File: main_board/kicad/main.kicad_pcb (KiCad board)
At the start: 2 copper layers, 200 x 150 mm, 148 parts, among them J1 Sensorbuchse, J2 Motorbuchse, J3 Motorbuchse, J4 Batteriebuchse, J5 Conn_02x07_Odd_Even, J6 Sensorbuchse, J7 AVR-ISP-10, Q1 IRFB3077, Q13 IRFB3077, Q14 IRFB3077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

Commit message: rerouted some lines, also added attiny
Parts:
- moved R3 316.3 mm to (40.0, 89.5), turned to 0 degrees
- moved R2 311.5 mm to (31.1, 90.2), turned to 90 degrees
- moved C3 311.2 mm to (34.9, 74.3), turned to 0 degrees
- moved U2 300.9 mm to (42.6, 85.1)
- moved R1 297.3 mm to (45.7, 69.8), turned to -90 degrees
- moved C4 292.1 mm to (42.5, 74.3), turned to 180 degrees
- moved J7 214.9 mm to (132.1, 34.3), turned to 90 degrees
- moved J1 133.5 mm to (219.6, 158.8), turned to 90 degrees
- moved J6 106.3 mm to (219.1, 52.1), turned to 90 degrees
- moved C22 65.7 mm to (163.2, 166.3), turned to 90 degrees
- moved C24 48.8 mm to (185.4, 75.6), turned to -90 degrees
- moved R26 47.7 mm to (175.9, 80.6), turned to 90 degrees
- moved C17 47.5 mm to (188.6, 75.6), turned to -90 degrees
- moved R28 46.8 mm to (185.4, 65.4), turned to -90 degrees
- moved C20 44.9 mm to (182.2, 70.4), turned to 90 degrees
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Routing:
- net +5V: track 74.1 -> 298.1 mm
- net GND: track 947.0 -> 1155.3 mm
- net /attiny13/SCK: track 0.00 -> 160.3 mm
- net /MotorMagic_R/HAL1: track 0.00 -> 101.1 mm
- net /MotorMagic_R/HAL2: track 0.00 -> 93.8 mm
- net /MotorMagic_R/HAL3: track 0.00 -> 88.6 mm
- net Net-(U5-A0): track 5.18 -> 68.4 mm
- net Net-(U5-A1): track 5.61 -> 65.1 mm
- net Net-(U5-A2): track 6.13 -> 62.9 mm
- net /BAT_CHARGE_PWM: track 0.00 -> 53.8 mm
- net /MotorMagic_R/bridge2/Y_L: track 74.5 -> 118.5 mm
- net /MotorMagic_L/HAL3: track 0.00 -> 43.8 mm
- net /MotorMagic_R/bridge2/Y_H: track 62.9 -> 104.9 mm
- net /MotorMagic_R/bridge2/G_H: track 87.9 -> 129.0 mm
- net /MotorMagic_R/bridge2/B_H: track 112.7 -> 153.6 mm
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
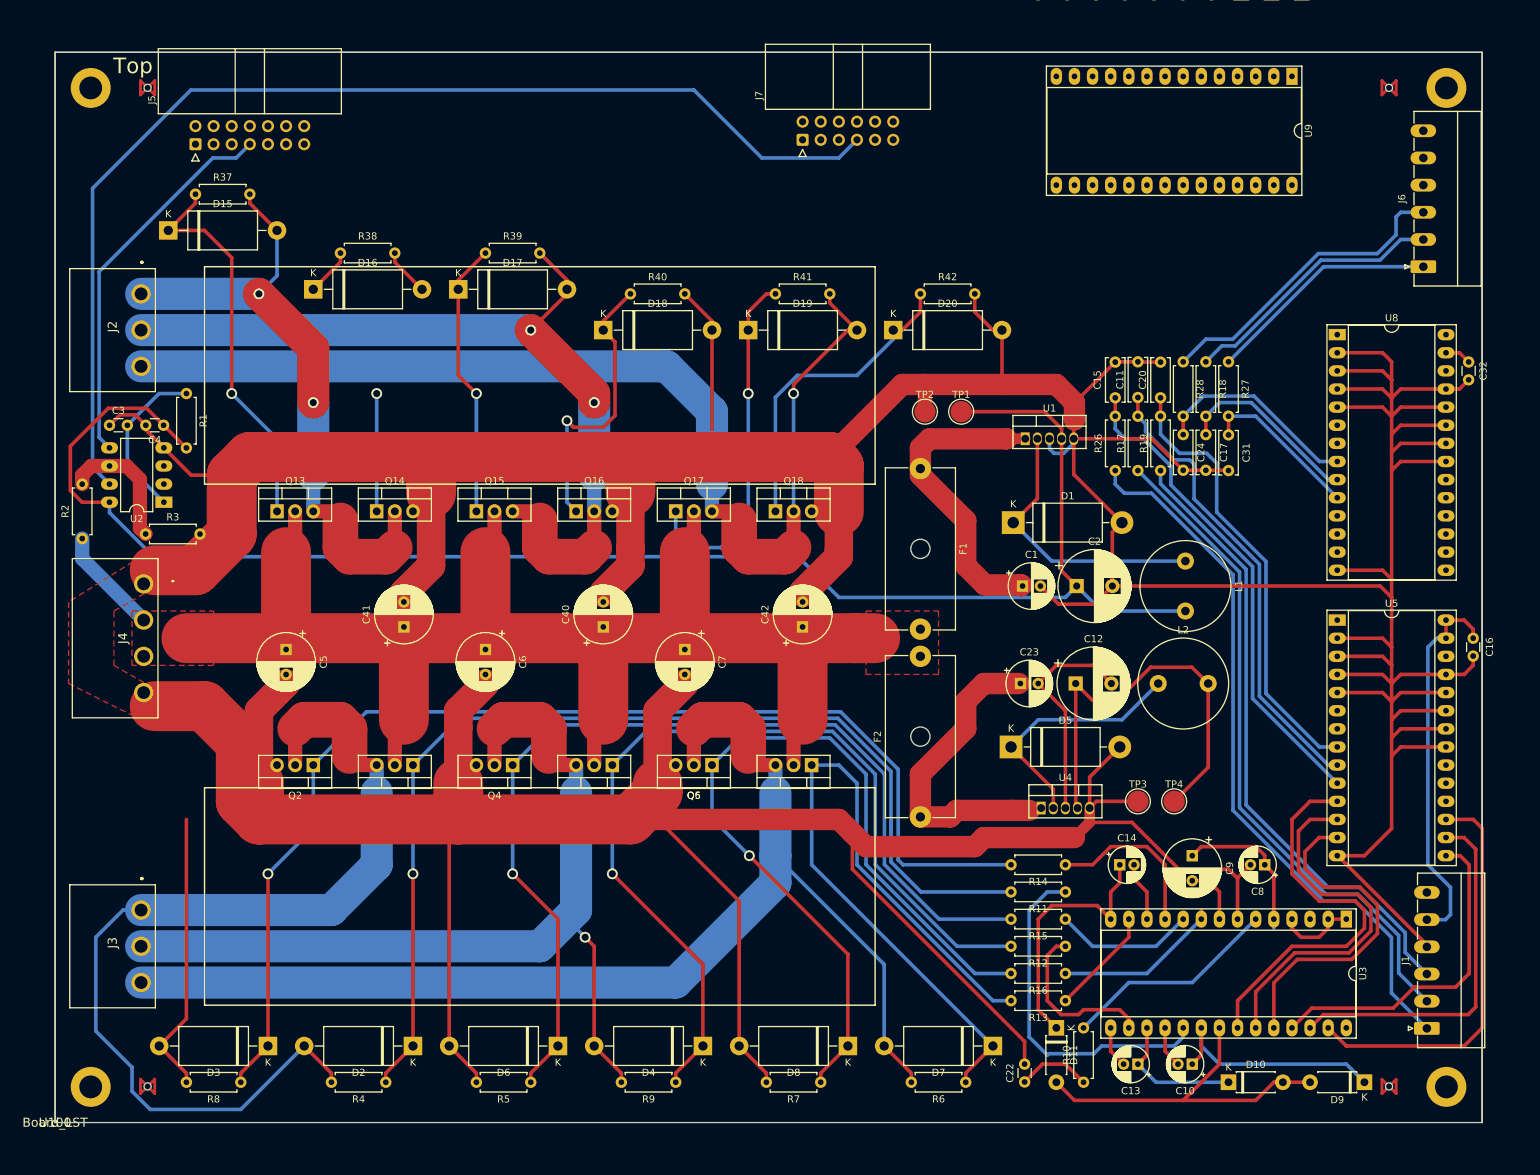
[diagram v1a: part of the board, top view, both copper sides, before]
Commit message: rerouted some lines
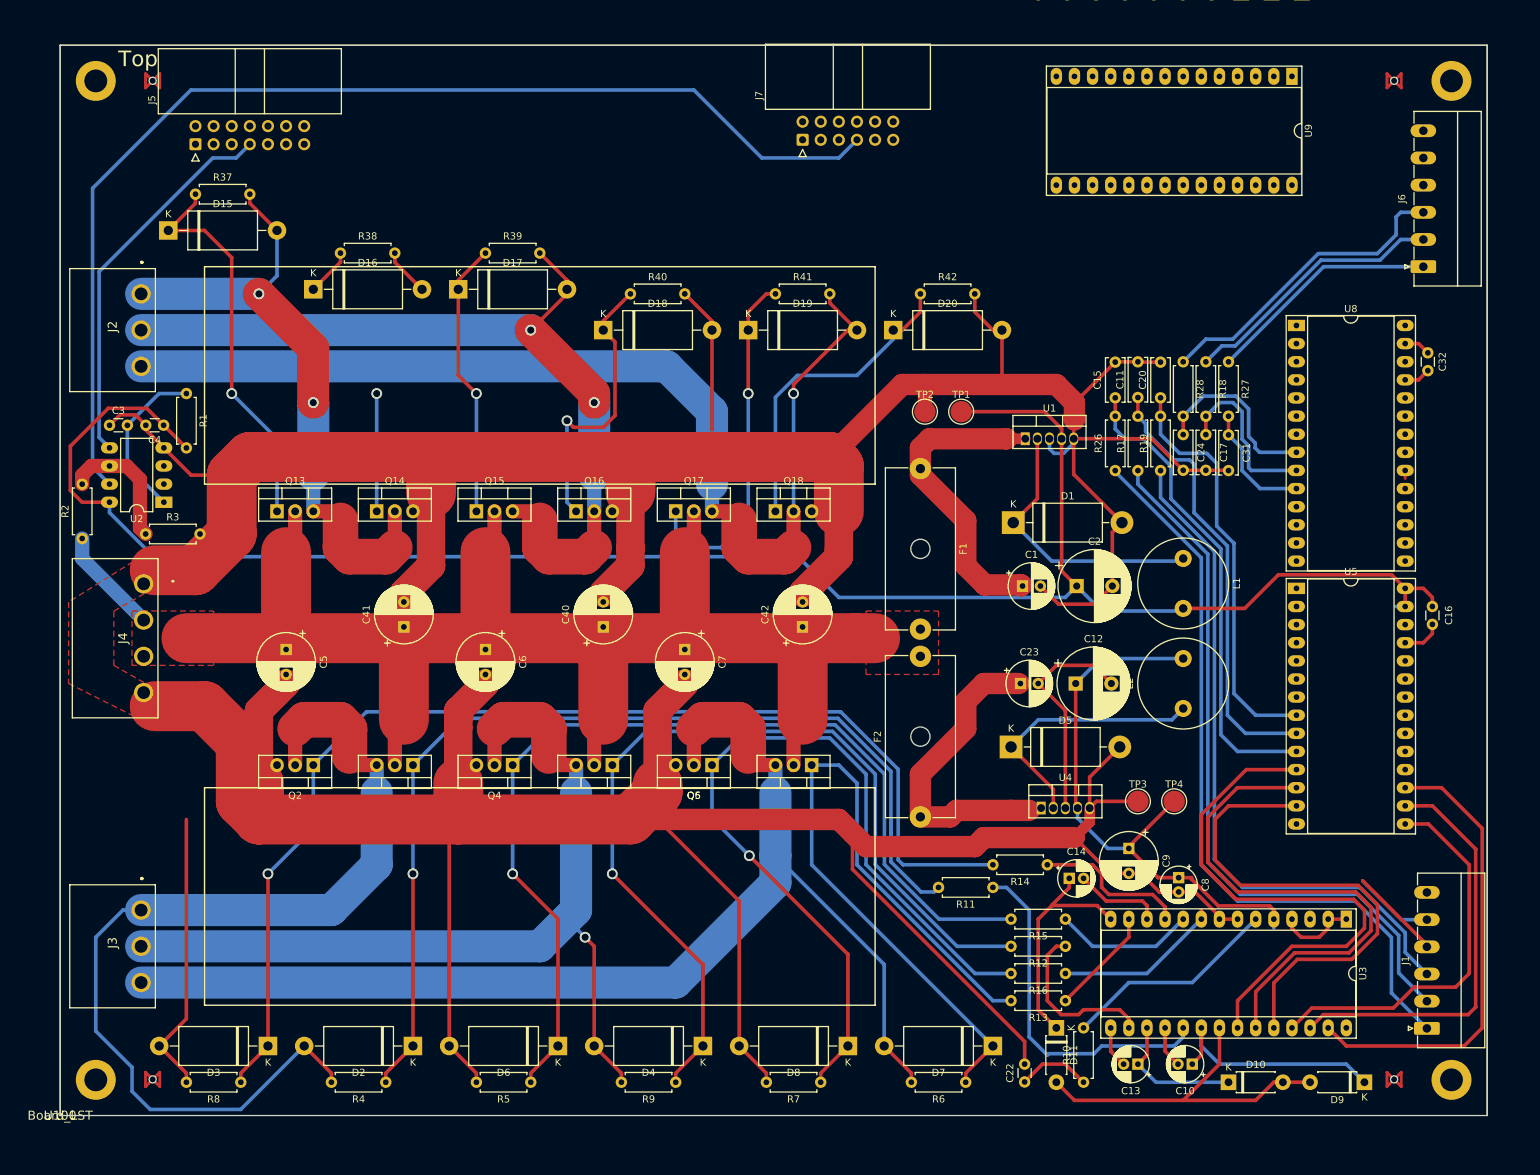
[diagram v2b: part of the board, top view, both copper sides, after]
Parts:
- moved C8 12.2 mm to (184.8, 137.7), turned to -90 degrees
- moved R11 10.2 mm to (158.8, 139.1)
- moved C9 8.95 mm to (177.8, 133.6)
- moved C14 7.33 mm to (169.4, 137.8)
- moved C16 7.24 mm to (220.3, 99.7)
- moved U5 7.24 mm to (201.3, 97.2)
- moved C32 5.86 mm to (219.7, 64.1)
- moved U8 5.86 mm to (201.3, 60.3)
- moved L2 4.95 mm to (185.4, 114.0), turned to 90 degrees
- moved R14 2.54 mm to (166.4, 135.9)
- moved U100 1.21 mm to (28.0, 171.0)
- moved L1 0.48 mm to (185.4, 93.0)
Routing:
- net GND: track 1155.3 -> 868.3 mm
- net /MotorMagic_R/bridgeDriver2/Y_H_IN: track 47.7 -> 71.0 mm
- net /MotorMagic_R/bridgeDriver2/G_H_IN: track 52.0 -> 73.9 mm
- net /MotorMagic_R/bridgeDriver2/B_H_IN: track 55.6 -> 76.8 mm
- net /MotorMagic_R/bridge2/B_H: track 153.6 -> 143.7 mm
- net /MotorMagic_R/bridgeDriver2/G_L_IN: track 51.4 -> 58.9 mm
- net /MotorMagic_R/bridgeDriver2/Y_L_IN: track 57.2 -> 64.8 mm
- net /MotorMagic_R/bridgeDriver2/B_L_IN: track 47.0 -> 54.6 mm
- net /MotorMagic_R/HAL2: track 93.8 -> 100.8 mm
- net /MotorMagic_R/HAL3: track 88.6 -> 95.7 mm
- net Net-(U8-A0): track 22.6 -> 17.1 mm
- net Net-(U5-A2): track 62.9 -> 58.0 mm
- net /MotorMagic_R/HAL1: track 101.1 -> 105.9 mm
- net /MotorMagic_R/Y_OUT: track 181.1 -> 185.1 mm
- net Net-(U8-A2): track 29.1 -> 25.5 mm
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
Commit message: rerouted lines
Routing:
- net +5V: track 298.8 -> 445.2 mm
- net GND: track 868.3 -> 989.8 mm
- net /DIR_R_REG: track 0.00 -> 71.7 mm
- net /PWM_R_REG: track 0.00 -> 66.8 mm
- net /MotorMagic_L/bridgeDriver2/Y_H_IN: track 0.00 -> 57.7 mm
- net /MotorMagic_L/bridgeDriver2/G_H_IN: track 0.00 -> 55.5 mm
- net /MotorMagic_L/bridgeDriver2/B_H_IN: track 0.00 -> 53.2 mm
- net /PWM_L_REG: track 0.00 -> 34.6 mm
- net /DIR_L_REG: track 0.00 -> 31.0 mm
- net +15V: track 130.2 -> 147.3 mm
- net /MotorMagic_R/bridgeDriver2/Y_L_IN: track 64.8 -> 58.2 mm
- net /ENABLE_R_REG: track 30.4 -> 36.4 mm
- net /MotorMagic_R/bridgeDriver2/G_L_IN: track 58.9 -> 54.0 mm
- net /MotorMagic_R/bridgeDriver2/B_L_IN: track 54.6 -> 51.8 mm
- net Net-(U3-LO3): track 23.5 -> 25.0 mm
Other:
- board text added: "Connect these next"
- board text added: "TODO"

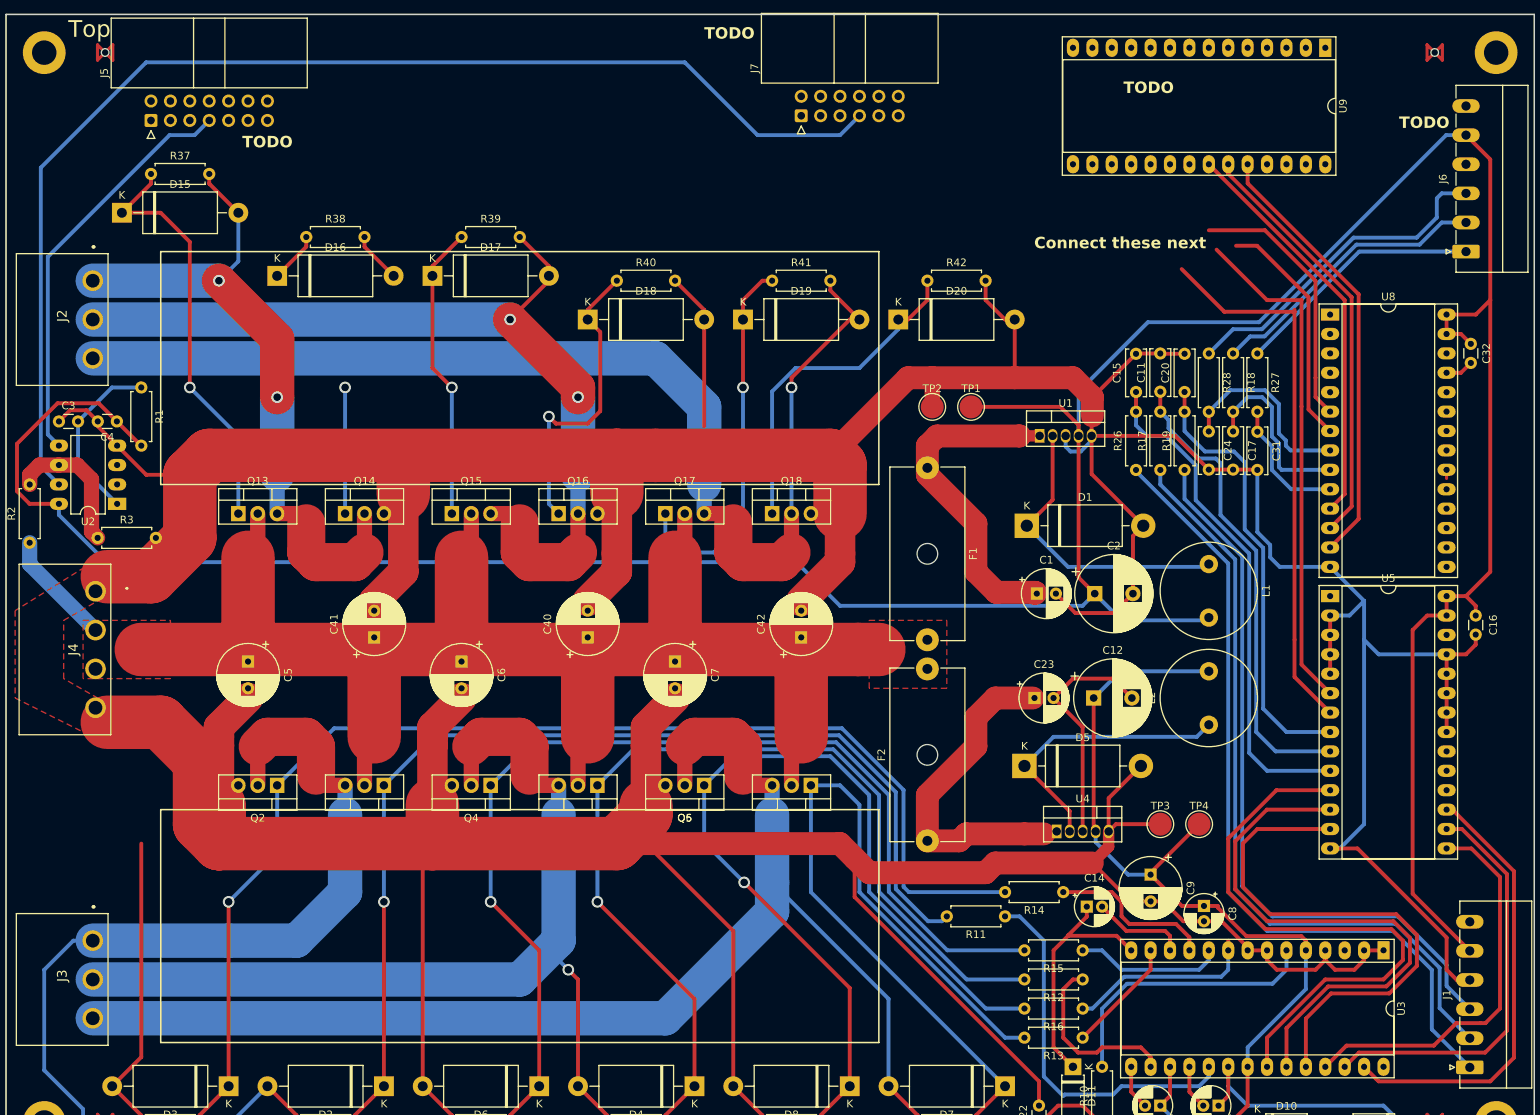
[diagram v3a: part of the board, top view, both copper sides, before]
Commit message: installed REG connector
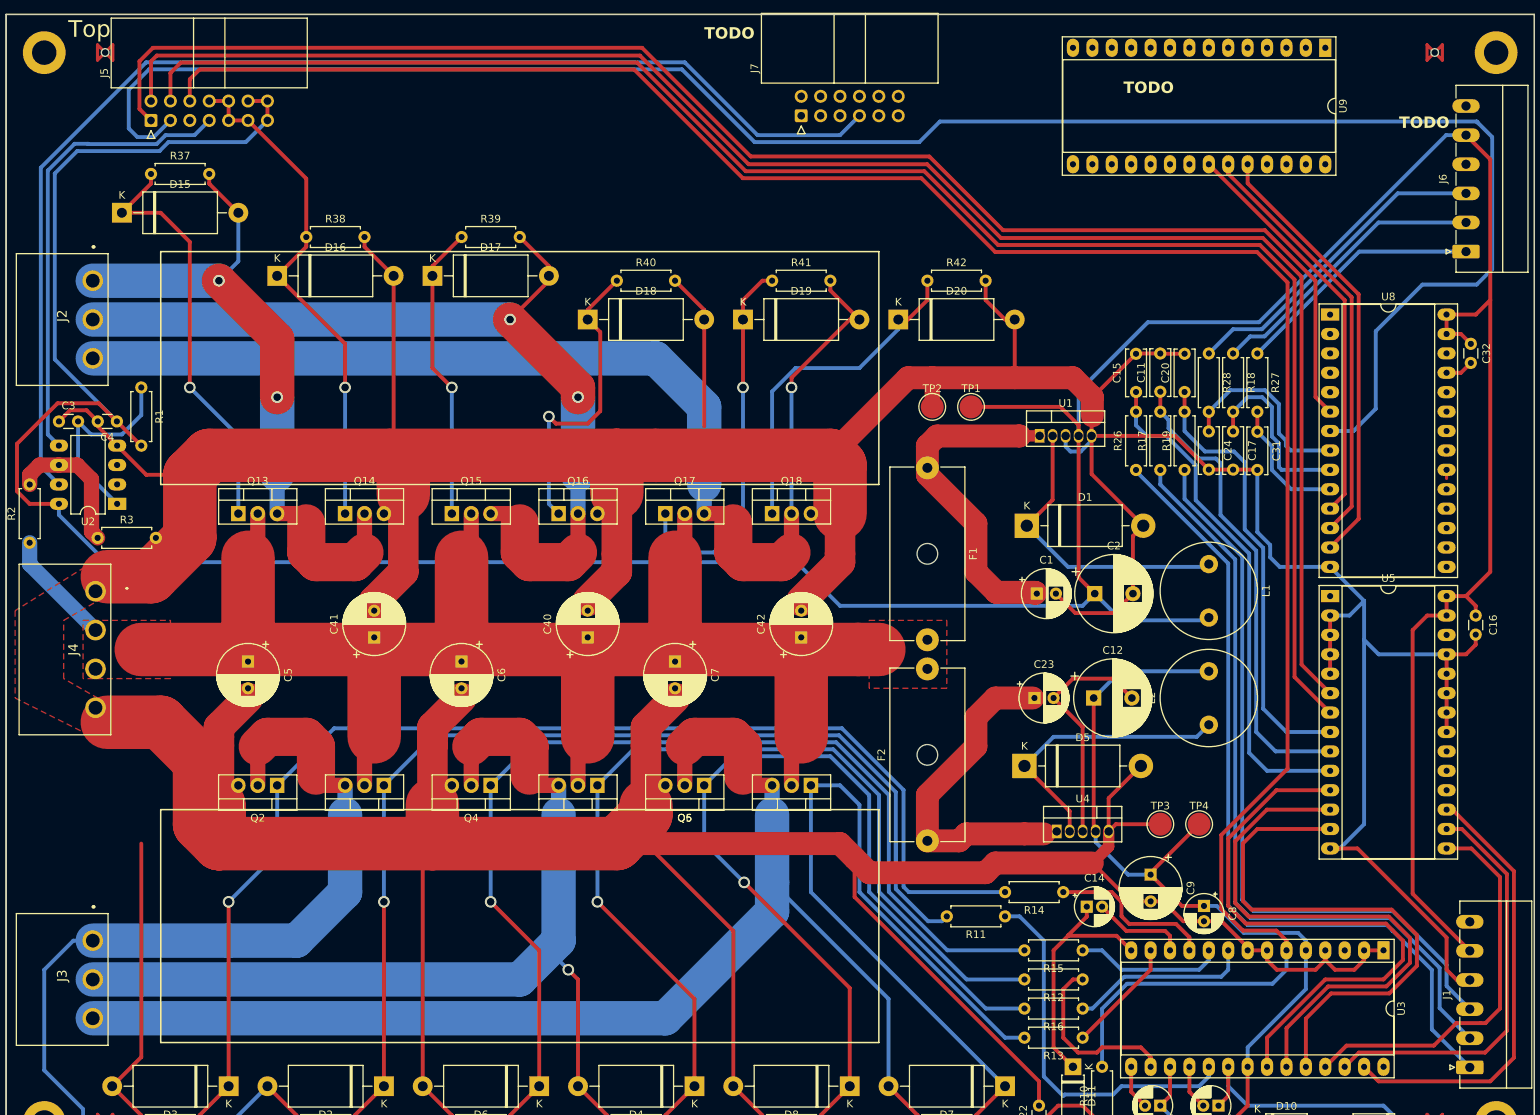
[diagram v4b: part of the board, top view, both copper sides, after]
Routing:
- net /ENABLE_R_REG: track 36.4 -> 292.0 mm
- net /DIR_L_REG: track 31.0 -> 250.8 mm
- net /PWM_L_REG: track 34.6 -> 193.5 mm
- net /PWM_R_REG: track 66.8 -> 224.1 mm
- net /DIR_R_REG: track 71.7 -> 221.7 mm
- net +5V: track 445.2 -> 516.8 mm
- net GND: track 989.8 -> 1039.5 mm
- net /MotorMagic_L/bridge2/B_L: track 16.5 -> 33.9 mm
- net /BAT_CHARGE_PWM: track 53.8 -> 60.5 mm
- net /attiny13//RESET: track 23.0 -> 26.5 mm
- net /MotorMagic_L/HAL3: track 43.8 -> 42.3 mm
- net Net-(U3-LO3): track 25.0 -> 23.7 mm
- net /MotorMagic_R/bridgeDriver2/B_H_IN: track 76.8 -> 77.9 mm
- net /MotorMagic_R/bridgeDriver2/Y_H_IN: track 71.0 -> 72.1 mm
- net /MotorMagic_R/bridgeDriver2/G_H_IN: track 73.9 -> 75.0 mm
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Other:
- board text removed: "Connect these next"

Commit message: rerouted more lines, also implemented HAL LEDS
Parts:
- moved R45 262.1 mm to (72.9, 44.7)
- moved R49 259.0 mm to (116.1, 41.1), turned to 90 degrees
- moved D26 257.1 mm to (123.4, 43.7)
- moved D22 255.1 mm to (73.4, 39.6)
- moved R44 254.4 mm to (83.1, 44.7)
- moved R47 252.2 mm to (119.4, 41.1), turned to 90 degrees
- moved D21 251.6 mm to (80.3, 39.6)
- moved U6 248.8 mm to (97.0, 44.7), turned to 90 degrees
- moved D25 247.9 mm to (130.3, 43.7)
- moved R48 245.2 mm to (125.7, 49.3)
- moved R46 244.2 mm to (93.5, 35.8), turned to -90 degrees
- moved D23 239.6 mm to (87.1, 39.6)
- moved D24 238.9 mm to (137.2, 43.7)
- moved R22 204.1 mm to (205.0, 46.7)
- moved R20 200.6 mm to (205.0, 43.4)
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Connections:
- J5 pad 7: /BAT_CHARGE_PWM -> /attiny13/Battery_Charge_PWM
- R38 pad 2: GND -> /MotorMagic_L/bridge2/B_L
- R8 pad 2: GND -> /MotorMagic_R/bridge2/B_L
- U2 pad 5: /BAT_CHARGE_PWM -> /attiny13/Battery_Charge_PWM
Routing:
- net GND: track 1039.5 -> 1458.5 mm
- net +5V: track 516.8 -> 891.9 mm
- net /MotorMagic_R/HAL1: track 107.0 -> 409.8 mm
- net /MotorMagic_R/HAL2: track 101.9 -> 387.7 mm
- net /MotorMagic_R/HAL3: track 96.7 -> 366.1 mm
- net /attiny13/Battery_Charge_PWM: track 0.00 -> 229.6 mm
- net /ENABLE_L_REG: track 0.00 -> 199.3 mm
- net /attiny13/MISO: track 18.7 -> 195.7 mm
- net /MotorMagic_L/HAL2: track 37.6 -> 210.6 mm
- net /MotorMagic_L/HAL3: track 42.3 -> 205.5 mm
- net /attiny13//RESET: track 26.5 -> 183.1 mm
- net +15V: track 147.2 -> 300.6 mm
- net Net-(U9-HO1): track 0.00 -> 132.0 mm
- net Net-(U9-HO2): track 0.00 -> 125.8 mm
- net /MotorMagic_L/HAL1: track 32.8 -> 154.3 mm
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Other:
- board text removed: "TODO"

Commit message: added text markers
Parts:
- moved D27 103.4 mm to (243.5, 86.6)
- moved R50 103.4 mm to (238.5, 76.3)
- moved D28 99.4 mm to (256.5, 78.7)
- moved D29 99.4 mm to (264.0, 78.7)
- moved D30 99.4 mm to (271.5, 78.7)
- moved R51 99.4 mm to (262.1, 88.7)
- moved R52 99.4 mm to (261.4, 66.7)
- moved R53 99.4 mm to (272.3, 89.0)
- moved R21 0.79 mm to (213.1, 57.0)
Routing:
- net GND: track 1458.5 -> 1472.1 mm
- net /MotorMagic_L/Y_OUT: track 162.3 -> 173.6 mm, vias 1 -> 0
- net +5V: track 891.9 -> 891.1 mm
- net /MotorMagic_L/HAL1: track 154.3 -> 155.1 mm
- net /MotorMagic_L/bridge2/G_L: track 105.6 -> 105.0 mm
- net /MotorMagic_L/bridge2/Y_H: vias 1 -> 0
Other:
- board text added: "ISP_ATTINY"
- board text added: "MOTOR_L"
- board text added: "MOTOR_R"
- board text added: "SENSOR_L"
- board text added: "SENSOR_R"
- board text added: "TO_REG"
